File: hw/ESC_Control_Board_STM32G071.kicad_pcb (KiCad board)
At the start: 6 copper layers, 50 x 67 mm, 90 parts, among them IC1 MCP2518FDT-E_SL, IC2 MCP2518FDT-E_SL, IC3 STM32G071RBT6, IC4 AZ1117CR-3.3TRG1, IC5 ISO1540QDRQ1, IC6 INA240A2PW, IC7 ADM3050EBRIZ, IC8 ADM3050EBRIZ, J1 Conn_ARM_JTAG_SWD_10, J2 Conn_01x03, J3 Conn_01x04, J4 Conn_01x04, J5 Conn_01x02, J6 Conn_01x15, U1 L6498DTR, U10 LNK306DN-TL, U2 L6498DTR, U3 L6498DTR, U4 ZXGD3006E6QTA, U5 ZXGD3006E6QTA, U6 ZXGD3006E6QTA, U7 ZXGD3006E6QTA, U8 ZXGD3006E6QTA, U9 ZXGD3006E6QTA, Y1 ABM8-20.000MHZ-10-B1U-T, Y2 ABM8-20.000MHZ-10-B1U-T

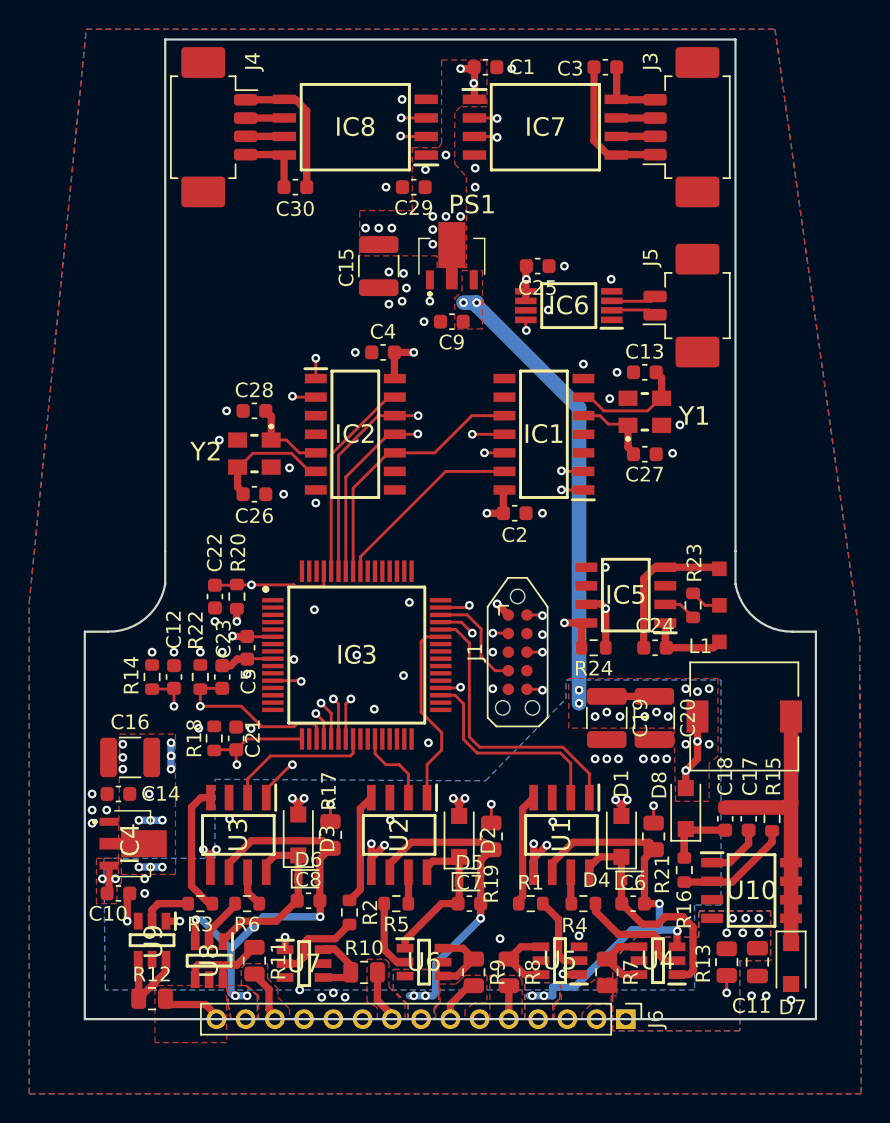
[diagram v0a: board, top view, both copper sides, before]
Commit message: connected interrupt pins to CAN controller
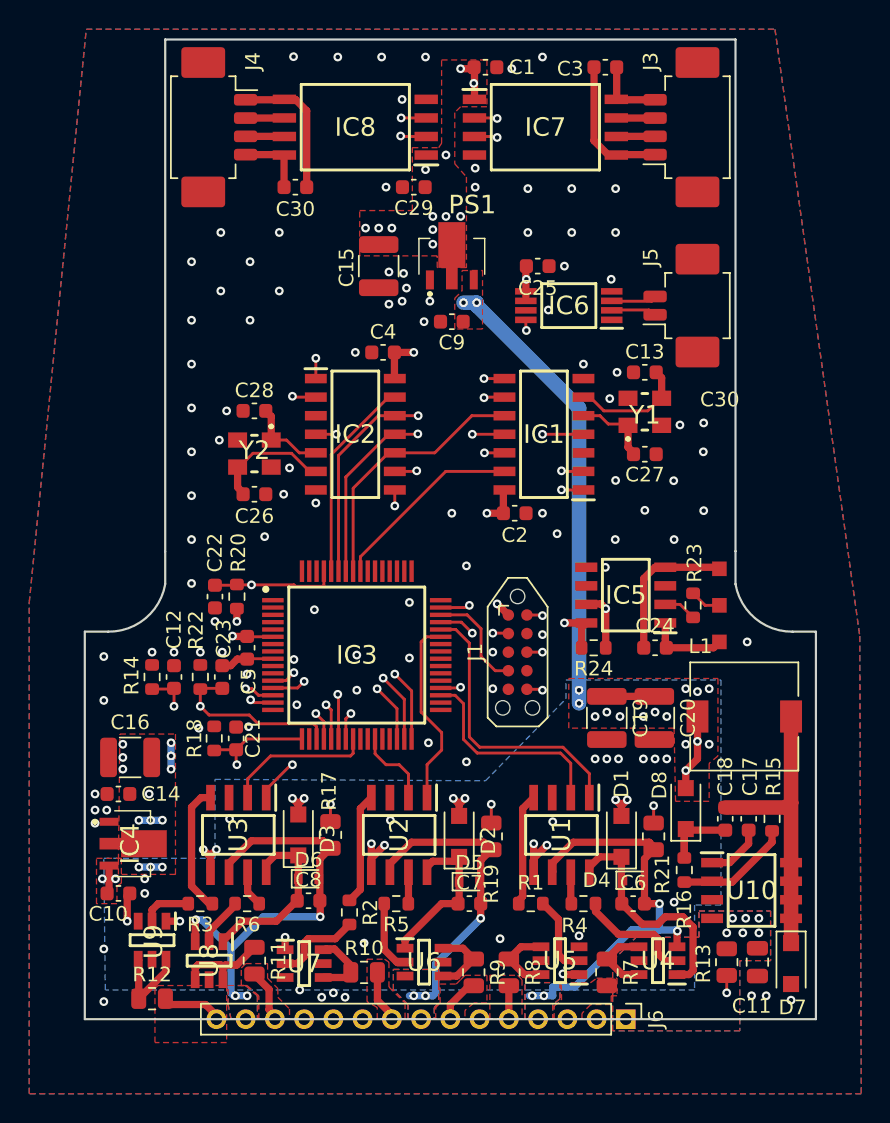
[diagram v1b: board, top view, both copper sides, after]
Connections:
- IC1 pad 4: unconnected-(IC1-Pad4) -> /CAN/CAN1_INT
- IC1 pad 8: unconnected-(IC1-Pad8) -> /CAN/CAN1_INT_RX
- IC1 pad 9: unconnected-(IC1-Pad9) -> /CAN/CAN1_INT_TX
- IC2 pad 4: unconnected-(IC2-Pad4) -> /CAN/CAN2_INT
- IC2 pad 8: unconnected-(IC2-Pad8) -> /CAN/CAN2_INT_RX
- IC2 pad 9: unconnected-(IC2-Pad9) -> /CAN/CAN2_INT_TX
- IC3 pad 13: /MCU/PC0 -> /CAN/CAN1_INT
- IC3 pad 14: /MCU/PC1 -> /CAN/CAN1_INT_TX
- IC3 pad 15: /MCU/PC2 -> /CAN/CAN1_INT_RX
- IC3 pad 28: /MCU/CAN1_EN -> unconnected-(IC3-Pad28)
- IC3 pad 30: unconnected-(IC3-Pad30) -> /CAN/CAN2_INT
- IC3 pad 31: unconnected-(IC3-Pad31) -> /CAN/CAN2_INT_TX
- IC3 pad 32: unconnected-(IC3-Pad32) -> /CAN/CAN2_INT_RX
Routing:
- net /CAN/CAN1_INT: track 0.00 -> 39.2 mm, vias 0 -> 2
- net /CAN/CAN1_INT_RX: track 0.00 -> 38.8 mm, vias 0 -> 2
- net /CAN/CAN1_INT_TX: track 0.00 -> 36.3 mm, vias 0 -> 2
- net /CAN/CAN2_INT: track 0.00 -> 29.6 mm, vias 0 -> 2
- net /CAN/CAN2_INT_TX: track 0.00 -> 21.4 mm, vias 0 -> 2
- net /CAN/CAN2_INT_RX: track 0.00 -> 17.5 mm, vias 0 -> 2
- net /MCU/CURR_SENSE: track 34.8 -> 39.1 mm
- net /MCU/INPUT_PIN: track 29.9 -> 31.0 mm
- net /MCU/VOLT_SENSE: track 64.7 -> 65.5 mm
- net GND: vias 75 -> 120
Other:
- board text added: "C30"

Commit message: Revision V1.0
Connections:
- IC3 pad 37: unconnected-(IC3-Pad37) -> /MCU/pV_HIGH
- IC3 pad 42: unconnected-(IC3-Pad42) -> /MCU/pU_HIGH
- IC3 pad 43: /MCU/pV_HIGH -> unconnected-(IC3-Pad43)
- IC3 pad 44: /MCU/pU_HIGH -> unconnected-(IC3-Pad44)
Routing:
- net /MCU/pV_HIGH: track 13.1 -> 10.1 mm
- net /MCU/pU_HIGH: track 19.7 -> 18.6 mm
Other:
- board text added: "STM32G071 CAN Control board V1.0"
- board text removed: "C30"
